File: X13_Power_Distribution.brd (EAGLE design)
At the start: 152.4 x 73.7 mm, 34 parts, among them Q1 310mA/60V/1.6Ω

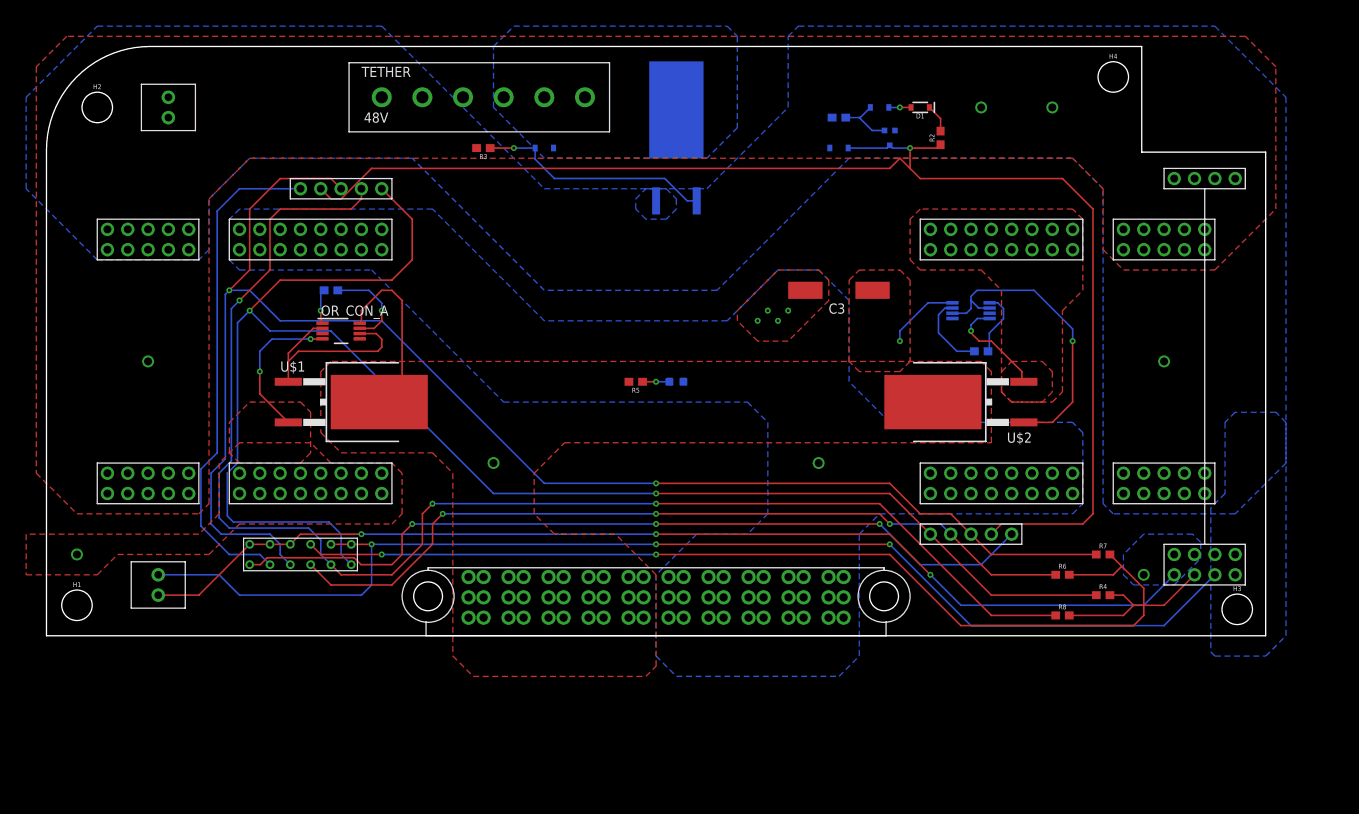
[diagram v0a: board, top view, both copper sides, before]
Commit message: Fixed some DRC errors
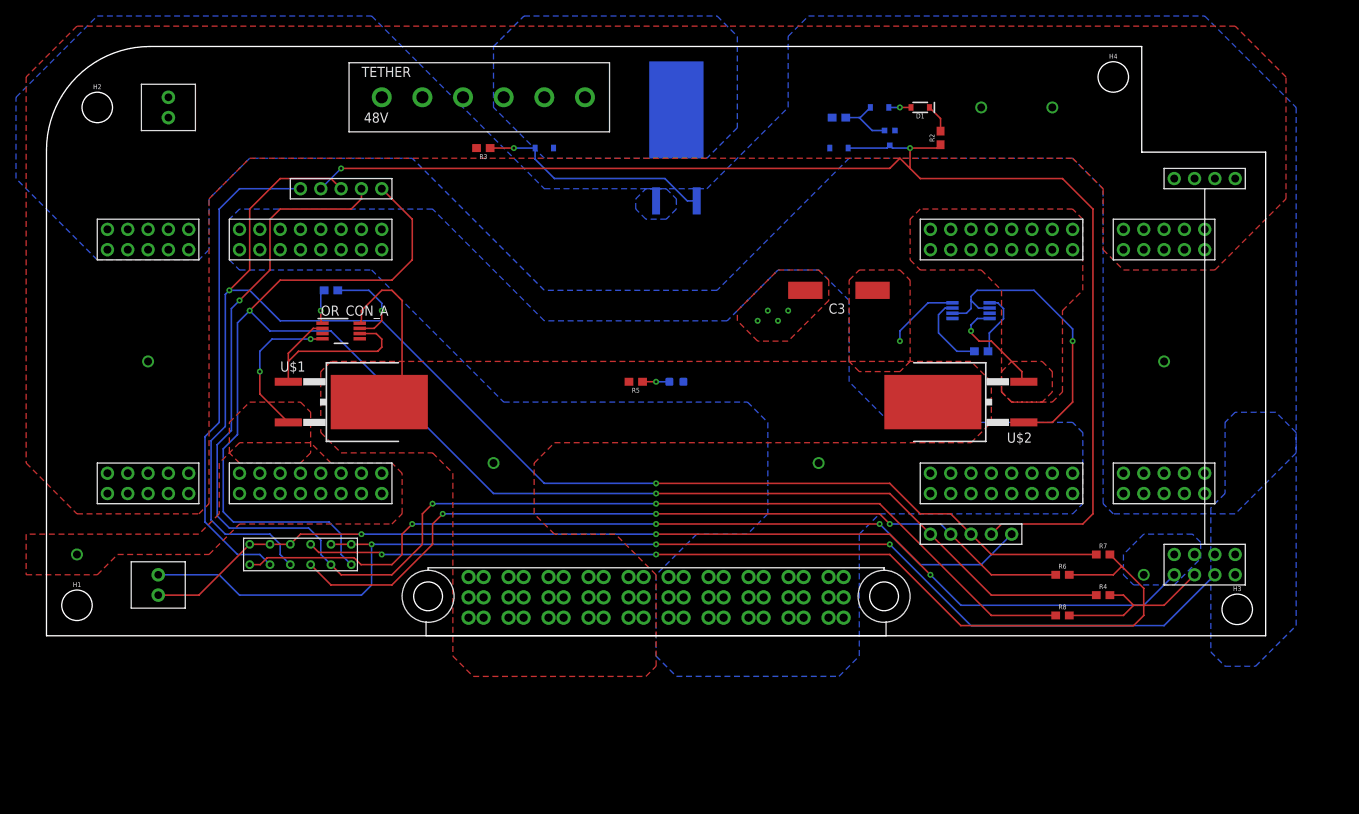
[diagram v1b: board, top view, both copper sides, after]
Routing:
- net ON/OFF: track 168.2 -> 167.1 mm, vias 1 -> 2
- net C2_1: track 62.4 -> 61.4 mm
- net +12V: track 33.8 -> 33.0 mm

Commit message: Exports and cleaning up git for ordering
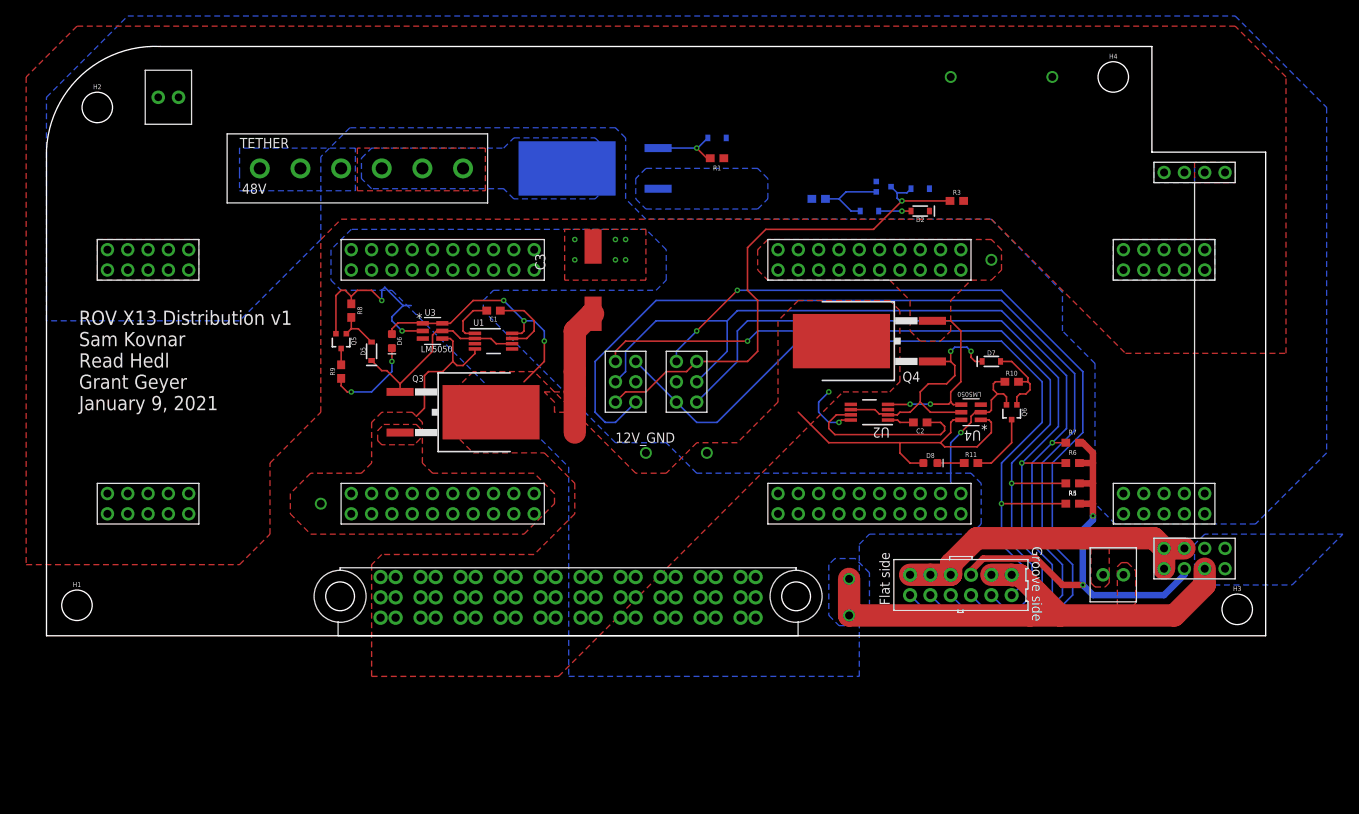
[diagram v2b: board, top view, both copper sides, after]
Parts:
- removed OR_CON_A, OR_CON_B: Value, Dist_OR_Controller:DGK0008A_M
- removed U$1, U$2, U$6: IRF1018EPBF, Reverse_Voltage_NMOS:TO263
- removed U$3, U$4: (no value), Brick_Dist_Connector:DIST2BRICK
- added BRICK1, BRICK2: DIST2BRICKVER_D2, Brick_Dist_Connector:DIST2BRICK_D2
- added D4: 5V, SparkFun-DiscreteSemi:SOD-323
- added D7: 15V, SparkFun-DiscreteSemi:SOD-323
- added D8: (no value), SparkFun-LED:LED-0603
- added Q2, Q5, Q6: SSM3K341R, SparkFun-DiscreteSemi:SOT323
- added Q3, Q4: IRF1018EPBF, Reverse_Voltage_NMOS:TO263
- added R10: 1M, SparkFun-Resistors:0603
- added R11, R9: 470, SparkFun-Resistors:0603
- added U1, U2: LM74610, Dist_OR_Controller:DGK0008A_M
- added U3, U4: LM5050, Dist_OR_Controller:MK06A-M
- BACKPLANE_LOGIC: value IPL1-107-01-L-D-RE-P -> IPL1-106-01-L-D-K; device Backplane_Dist_Logic_Connector:IPL1-107-01-L-D-RE-P -> Backplane_Dist_Logic_Connector:IPL1-106-01-L-D-K
- C1, C2: value (none) -> 2.2uF
- D1: value 22V -> 15V
- D2: value 5V -> 22V
- D5: value (none) -> 15V; device SparkFun-LED:LED-0603 -> SparkFun-DiscreteSemi:SOD-323
- D6: value 15V -> (none); device SparkFun-DiscreteSemi:SOD-323 -> SparkFun-LED:LED-0603
- Q1: value 310mA/60V/1.6Ω -> IRF1018EPBF; device SparkFun-DiscreteSemi:SOT323 -> Reverse_Voltage_NMOS:TO263
- R2, R8: value 10k -> 1M
- R3: value 1M -> 10k
- R5: value 470 -> 10k
- moved 5V_POE 118.1 mm to (132.1, 7.62), turned to 0 degrees
- moved R8 96.7 mm to (38.1, 40.6), turned to 270 degrees
- moved BACKPLANE_LOGIC 82.6 mm to (108.0, 7.62)
- moved R3 59.5 mm to (113.8, 54.4), turned to 0 degrees
- moved R5 56.1 mm to (128.3, 19.1), turned to 0 degrees
- moved D5 38.3 mm to (40.6, 35.6), flipped to the top, turned to 90 degrees
- moved Q1 35.8 mm to (69.8, 58.4), turned to 270 degrees
- moved C3 30.8 mm to (68.3, 44.5), turned to 90 degrees
- moved D6 30.7 mm to (43.2, 36.8), flipped to the top, turned to 270 degrees
- moved D1 25.7 mm to (83.8, 62.2), flipped to the bottom
- moved C1 20.5 mm to (55.9, 40.6), flipped to the top, turned to 180 degrees
- moved TETHER 17.6 mm to (26.7, 58.4)
- moved R2 17.0 mm to (96.5, 54.6), flipped to the bottom, turned to 180 degrees
- moved R1 16.1 mm to (83.8, 59.7), flipped to the top, turned to 0 degrees
- moved R7 14.5 mm to (128.3, 24.1)
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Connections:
- removed net N$8: D5.A, R5.1
- new net LED_DRIVE_A: D5.A, Q5.1, R8.2
- new net LED_DRIVE_B: D7.A, Q6.1, R10.2
- new net N$4: Q5.3, R9.2
- new net N$5: D6.C, R9.1
- new net N$6: Q6.3, R11.2
- new net N$7: D8.C, R11.1
- net +12V: now also D6.A, D8.A, Q3.3, Q4.3, U1.8, U2.8, U3.1, U3.6, U4.1, U4.6; no longer OR_CON_A.8, OR_CON_B.8, R5.2, U$1.3, U$2.3
- net +12V_A: now also BRICK1.2@1, BRICK1.2@10, BRICK1.2@11, BRICK1.2@12, BRICK1.2@13, BRICK1.2@14, BRICK1.2@15, BRICK1.2@16, BRICK1.2@17, BRICK1.2@18, BRICK1.2@19, BRICK1.2@2, BRICK1.2@20, BRICK1.2@3, BRICK1.2@4, BRICK1.2@5, BRICK1.2@6, BRICK1.2@7, BRICK1.2@8, BRICK1.2@9, Q3.2, U1.4, U3.4; no longer OR_CON_A.4, U$1.2, U$3.2@1, U$3.2@10, U$3.2@11, U$3.2@12, U$3.2@13, U$3.2@14, U$3.2@15, U$3.2@16, U$3.2@2, U$3.2@3, U$3.2@4, U$3.2@5, U$3.2@6, U$3.2@7, U$3.2@8, U$3.2@9
- net +12V_B: now also BRICK2.2@1, BRICK2.2@10, BRICK2.2@11, BRICK2.2@12, BRICK2.2@13, BRICK2.2@14, BRICK2.2@15, BRICK2.2@16, BRICK2.2@17, BRICK2.2@18, BRICK2.2@19, BRICK2.2@2, BRICK2.2@20, BRICK2.2@3, BRICK2.2@4, BRICK2.2@5, BRICK2.2@6, BRICK2.2@7, BRICK2.2@8, BRICK2.2@9, Q4.2, U2.4, U4.4; no longer OR_CON_B.4, U$2.2, U$4.2@1, U$4.2@10, U$4.2@11, U$4.2@12, U$4.2@13, U$4.2@14, U$4.2@15, U$4.2@16, U$4.2@2, U$4.2@3, U$4.2@4, U$4.2@5, U$4.2@6, U$4.2@7, U$4.2@8, U$4.2@9
- net +3.3V: now also R5.2; no longer R8.2
- net +48V: now also BRICK1.1@1, BRICK1.1@10, BRICK1.1@2, BRICK1.1@3, BRICK1.1@4, BRICK1.1@5, BRICK1.1@6, BRICK1.1@7, BRICK1.1@8, BRICK1.1@9, BRICK2.1@1, BRICK2.1@10, BRICK2.1@2, BRICK2.1@3, BRICK2.1@4, BRICK2.1@5, BRICK2.1@6, BRICK2.1@7, BRICK2.1@8, BRICK2.1@9, D2.C, R1.2; no longer D1.C, R2.2, U$3.1@1, U$3.1@10, U$3.1@2, U$3.1@3, U$3.1@4, U$3.1@5, U$3.1@6, U$3.1@7, U$3.1@8, U$3.1@9, U$4.1@1, U$4.1@10, U$4.1@2, U$4.1@3, U$4.1@4, U$4.1@5, U$4.1@6, U$4.1@7, U$4.1@8, U$4.1@9
- net 12V_GND: now also BRICK1.4@1, BRICK1.4@10, BRICK1.4@11, BRICK1.4@12, BRICK1.4@13, BRICK1.4@14, BRICK1.4@15, BRICK1.4@16, BRICK1.4@17, BRICK1.4@18, BRICK1.4@19, BRICK1.4@2, BRICK1.4@20, BRICK1.4@3, BRICK1.4@4, BRICK1.4@5, BRICK1.4@6, BRICK1.4@7, BRICK1.4@8, BRICK1.4@9, BRICK2.4@1, BRICK2.4@10, BRICK2.4@11, BRICK2.4@12, BRICK2.4@13, BRICK2.4@14, BRICK2.4@15, BRICK2.4@16, BRICK2.4@17, BRICK2.4@18, BRICK2.4@19, BRICK2.4@2, BRICK2.4@20, BRICK2.4@3, BRICK2.4@4, BRICK2.4@5, BRICK2.4@6, BRICK2.4@7, BRICK2.4@8, BRICK2.4@9, Q5.2, Q6.2, R10.1, R8.1, U3.2, U4.2; no longer D5.C, U$3.4@1, U$3.4@10, U$3.4@11, U$3.4@12, U$3.4@13, U$3.4@14, U$3.4@15, U$3.4@16, U$3.4@2, U$3.4@3, U$3.4@4, U$3.4@5, U$3.4@6, U$3.4@7, U$3.4@8, U$3.4@9, U$4.4@1, U$4.4@10, U$4.4@11, U$4.4@12, U$4.4@13, U$4.4@14, U$4.4@15, U$4.4@16, U$4.4@2, U$4.4@3, U$4.4@4, U$4.4@5, U$4.4@6, U$4.4@7, U$4.4@8, U$4.4@9
- net 48V_GND: now also BRICK1.3@1, BRICK1.3@10, BRICK1.3@2, BRICK1.3@3, BRICK1.3@4, BRICK1.3@5, BRICK1.3@6, BRICK1.3@7, BRICK1.3@8, BRICK1.3@9, BRICK2.3@1, BRICK2.3@10, BRICK2.3@2, BRICK2.3@3, BRICK2.3@4, BRICK2.3@5, BRICK2.3@6, BRICK2.3@7, BRICK2.3@8, BRICK2.3@9, D1.A, D4.A, Q2.2, R2.1; no longer D2.A, R1.1, U$3.3@1, U$3.3@10, U$3.3@2, U$3.3@3, U$3.3@4, U$3.3@5, U$3.3@6, U$3.3@7, U$3.3@8, U$3.3@9, U$4.3@1, U$4.3@10, U$4.3@2, U$4.3@3, U$4.3@4, U$4.3@5, U$4.3@6, U$4.3@7, U$4.3@8, U$4.3@9, U$6.2
- net ALERT_1: now also BRICK1.D, R5.1; no longer R8.1, U$3.D
- net ALERT_2: now also BRICK2.D; no longer U$4.D
- net C2_1: now also BRICK1.A; no longer U$3.A
- net C2_2: now also BRICK2.A; no longer U$4.A
- net CLK: now also BRICK1.C, BRICK2.C; no longer U$3.C, U$4.C
- net DATA: now also BRICK1.E, BRICK2.E; no longer U$3.E, U$4.E
- net GND_RAW: now also Q1.3; no longer D6.A, U$6.3
- net N$1: now also D2.A; no longer D1.A
- net ON/OFF: now also BRICK1.B, BRICK2.B, D4.C, Q2.3, R3.1; no longer D2.C, Q1.3, R2.1, U$3.B, U$4.B
- net ON/OFF_DRIVE: now also Q2.1, R2.2; no longer Q1.1, R1.2
- net OR_DRIVE_A: now also D5.C, Q3.1, U1.2, U1.6, U3.5; no longer OR_CON_A.2, OR_CON_A.6, U$1.1
- net OR_DRIVE_B: now also D7.C, Q4.1, U2.2, U2.6, U4.5; no longer OR_CON_B.2, OR_CON_B.6, U$2.1
- net REV_DRIVE: now also D1.C, Q1.1, R1.1; no longer D6.C, R3.1, U$6.1
- net VCAPH_A: now also U1.7; no longer OR_CON_A.7
- net VCAPH_B: now also U2.7; no longer OR_CON_B.7
- net VCAPL_A: now also U1.1; no longer OR_CON_A.1
- net VCAPL_B: now also U2.1; no longer OR_CON_B.1
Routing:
- net DATA: track 200.7 -> 98.7 mm, vias 2 -> 1
- net ON/OFF: track 167.1 -> 66.1 mm, vias 2 -> 1
- net +5V: track 135.4 -> 40.0 mm, vias 4 -> 0
- net +3.3V: track 146.5 -> 55.8 mm
- net 5V_GND: track 150.7 -> 66.7 mm, vias 3 -> 2
- net ALERT_1: track 174.2 -> 102.1 mm, vias 3 -> 2
- net CLK: track 189.4 -> 120.7 mm, vias 2 -> 1
- net C2_1: track 61.4 -> 129.1 mm
- net +12V: track 33.0 -> 95.3 mm, vias 2 -> 6
- net 12V_GND: track 0.00 -> 45.7 mm, vias 5 -> 10
- net REV_DRIVE: track 29.4 -> 8.96 mm
- net VCAPH_B: track 9.80 -> 21.8 mm
- net N$5: track 0.00 -> 11.6 mm, vias 0 -> 2
- net LED_DRIVE_B: track 0.00 -> 10.1 mm
- net C2_2: track 103.2 -> 113.1 mm, vias 3 -> 2
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- added copper zone on layer 1, net +5V
- added copper zone on layer 1, net 5V_GND
- removed copper zone on layer 16, net +5V
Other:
- outline, holes or cut-outs redrawn
- board text added: "+12V_B"
- board text added: "48V_ETHERNET"
- board text added: "LM74610"
- board text added: "ROV X13 Distribution v1 Sam Kovnar Read Hedl Grant Geyer January 9, 2021"
- board text removed: "+5V"

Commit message: playing with 3d package generator in eagle
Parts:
- Q1, Q3, Q4: device Reverse_Voltage_NMOS:TO263 -> Dist_Reverse_Voltage_NMOS:TO263
- moved Q3 0.25 mm to (50.8, 27.7), turned to 0 degrees
- turned Q1 to 0 degrees
- turned Q4 to 180 degrees
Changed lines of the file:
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@@
 <setting verticaltext="up"/>
 </settings>
-<grid distance="50" unitdist="mil" unit="mil" style="lines" multiple="1" display="yes" altdistance="10" altunitdist="mil" altunit="mil"/>
+<grid distance="10" unitdist="mil" unit="mil" style="lines" multiple="1" display="yes" altdistance="5" altunitdist="mil" altunit="mil"/>
 <layers>
 <layer number="1" name="Top" color="4" fill="1" visible="yes" active="yes"/>
@@
 <attribute name="PROD_ID" value=" " x="143.51" y="-45.72" size="1.778" layer="27" display="off"/>
 </element>
-<element name="Q1" library="Reverse_Voltage_NMOS" package="TO263" value="IRF1018EPBF" x="69.85" y="58.42" smashed="yes" rot="MR270">
-<attribute name="NAME" x="57.15" y="63.5" size="1.27" layer="26" ratio="15" rot="MR270"/>
-<attribute name="VALUE" x="80.518" y="64.262" size="1.27" layer="28" ratio="15" rot="MR270"/>
+<element name="Q1" library="Dist_Reverse_Voltage_NMOS" package="TO263" package3d_urn="urn:adsk.eagle:package:25914649/1" value="IRF1018EPBF" x="69.85" y="58.42" smashed="yes" rot="MR0">
+<attribute name="NAME" x="74.93" y="71.12" size="1.27" layer="26" ratio="15" rot="MR0"/>
+<attribute name="VALUE" x="75.692" y="47.752" size="1.27" layer="28" ratio="15" rot="MR0"/>
 </element>
 <element name="48V_POE" library="Dist_POE" package="CONN2_282834-2_TEC" value="POE_TERMINAL" x="13.97" y="67.31" smashed="yes">
@@
 <attribute name="TYPE" value="TYPE" x="102.87" y="27.94" size="1.778" layer="27" rot="R180" display="off"/>
 </element>
-<element name="Q3" library="Reverse_Voltage_NMOS" package="TO263" value="IRF1018EPBF" x="50.8" y="27.94" smashed="yes" rot="R270">
-<attribute name="NAME" x="45.72" y="31.75" size="0.8128" layer="25" ratio="15"/>
-<attribute name="VALUE" x="62.738" y="33.528" size="1.27" layer="27" ratio="15" rot="SR270"/>
-</element>
-<element name="Q4" library="Reverse_Voltage_NMOS" package="TO263" value="IRF1018EPBF" x="104.14" y="36.83" smashed="yes" rot="R90">
-<attribute name="NAME" x="109.22" y="33.02" size="1.27" layer="25" ratio="15" rot="R180"/>
-<attribute name="VALUE" x="91.44" y="41.91" size="1.27" layer="27" ratio="15" rot="R270"/>
+<element name="Q3" library="Dist_Reverse_Voltage_NMOS" package="TO263" package3d_urn="urn:adsk.eagle:package:25914649/1" value="IRF1018EPBF" x="50.8" y="27.686" smashed="yes">
+<attribute name="NAME" x="46.99" y="22.606" size="0.8128" layer="25" ratio="15" rot="R90"/>
+<attribute name="VALUE" x="45.212" y="39.624" size="1.27" layer="27" ratio="15" rot="SR0"/>
+</element>
+<element name="Q4" library="Dist_Reverse_Voltage_NMOS" package="TO263" package3d_urn="urn:adsk.eagle:package:25914649/1" value="IRF1018EPBF" x="104.14" y="36.83" smashed="yes" rot="R180">
+<attribute name="NAME" x="107.95" y="41.91" size="1.27" layer="25" ratio="15" rot="R270"/>
+<attribute name="VALUE" x="99.06" y="24.13" size="1.27" layer="27" ratio="15"/>
 </element>
 <element name="D4" library="SparkFun-DiscreteSemi" library_urn="urn:adsk.eagle:library:514" package="SOD-323" package3d_urn="urn:adsk.eagle:package:38441/1" value="5V" x="109.22" y="55.88" smashed="yes" rot="MR180">
@@
 <wire x1="46.9748" y1="39.116" x2="47.0408" y2="39.05" width="0.2032" layer="1"/>
 <wire x1="68.326" y1="40.25" x2="68.19" y2="40.25" width="2.794" layer="1"/>
-<wire x1="66.04" y1="38.1" x2="66.04" y2="33.02" width="2.794" layer="1"/>
-<wire x1="66.04" y1="33.02" x2="66.04" y2="30.48" width="2.794" layer="1"/>
-<wire x1="66.04" y1="25.4" x2="66.04" y2="30.48" width="2.794" layer="1"/>
+<wire x1="66.04" y1="38.1" x2="66.04" y2="25.4" width="2.794" layer="1"/>
 <wire x1="68.19" y1="40.25" x2="66.04" y2="38.1" width="2.794" layer="1"/>
 <via x="82.55" y="22.86" extent="1-16" drill="1"/>
 <wire x1="107.95" y1="21.59" x2="109.613" y2="21.59" width="0.2032" layer="1"/>
-<wire x1="66.04" y1="30.48" x2="66.04" y2="30.48" width="2.794" layer="1"/>
 <polygon width="0.254" layer="1">
 <vertex x="62.23" y="30.48"/>
@@
 <vertex x="63.5" y="29.21"/>
 </polygon>
-<wire x1="55.57" y1="27.94" x2="59.69" y2="31.75" width="0" layer="19" extent="1-1"/>
+<wire x1="55.618" y1="27.686" x2="59.69" y2="31.75" width="0" layer="19" extent="1-1"/>
 </signal>
 <signal name="+12V_A">
@@
 <contactref element="BRICK2" pad="2@5"/>
 <contactref element="BRICK2" pad="2@15"/>
-<wire x1="113.03" y1="39.37" x2="110.74" y2="39.37" width="0.2032" layer="1"/>
+<wire x1="113.03" y1="39.37" x2="110.692" y2="39.37" width="0.2032" layer="1"/>
 <wire x1="114.3508" y1="28.89" x2="113.35" y2="28.89" width="0.2032" layer="1"/>
 <wire x1="113.35" y1="28.89" x2="113.03" y2="29.21" width="0.2032" layer="1"/>
@@
 <wire x1="82.97" y1="59.69" x2="82.55" y2="59.69" width="0.2032" layer="1"/>
 <wire x1="82.55" y1="59.69" x2="81.28" y2="60.96" width="0.2032" layer="1"/>
-<wire x1="81.28" y1="60.96" x2="76.45" y2="60.96" width="0.2032" layer="16"/>
+<wire x1="81.28" y1="60.96" x2="76.402" y2="60.96" width="0.2032" layer="16"/>
 <via x="81.28" y="60.96" extent="1-16" drill="0.35"/>
 <wire x1="81.28" y1="60.96" x2="81.4" y2="60.96" width="0.2032" layer="16"/>
@@
 <wire x1="56.205" y1="36.505" x2="58.205003125" y2="36.505" width="0.2032" layer="1"/>
 <wire x1="55.555003125" y1="37.154996875" x2="56.205" y2="36.505" width="0.2032" layer="1"/>
-<wire x1="44.2" y1="30.48" x2="44.2" y2="31.5" width="0.2032" layer="1"/>
+<wire x1="44.248" y1="30.226" x2="44.2" y2="31.5" width="0.2032" layer="1"/>
 <wire x1="49.4792" y1="38.1" x2="50.8" y2="38.1" width="0.2032" layer="1"/>
 <wire x1="51.745003125" y1="37.154996875" x2="53.555" y2="37.154996875" width="0.2032" layer="1"/>
@@
 <wire x1="113.538" y1="33.782" x2="113.538" y2="32.512" width="0.2032" layer="1"/>
 <wire x1="113.538" y1="33.782" x2="113.03" y2="34.29" width="0.2032" layer="1"/>
-<wire x1="113.03" y1="34.29" x2="110.74" y2="34.29" width="0.2032" layer="1"/>
+<wire x1="113.03" y1="34.29" x2="110.692" y2="34.29" width="0.2032" layer="1"/>
 <wire x1="110.236" y1="31.496" x2="112.522" y2="31.496" width="0.2032" layer="1"/>
 <wire x1="114.3508" y1="27.94" x2="110.49" y2="27.94" width="0.2032" layer="1"/>
